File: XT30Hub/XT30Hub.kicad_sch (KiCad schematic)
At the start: 12 parts, among them J1 Conn_01x02, J2 Conn_01x02, J3 Conn_01x02, J4 Conn_01x02, J5 Conn_01x02, J6 Conn_01x02

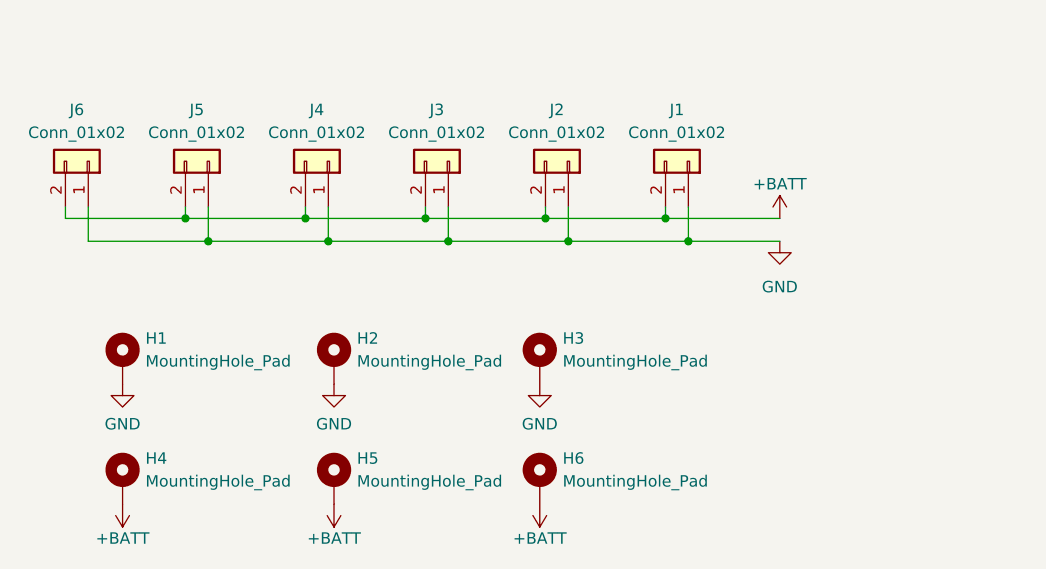
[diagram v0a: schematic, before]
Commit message: [XT30Hub] : 回路図をPDF化
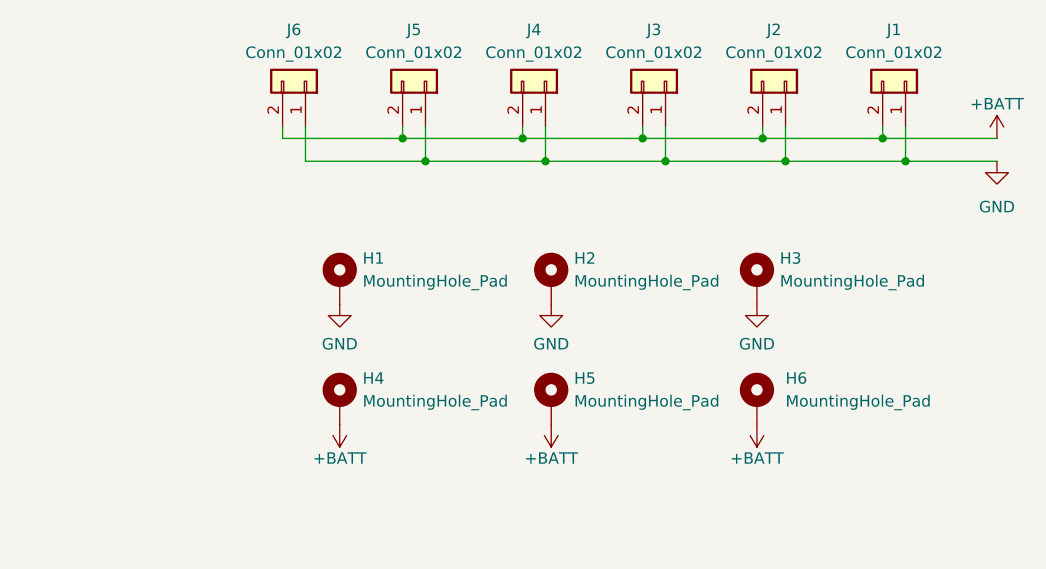
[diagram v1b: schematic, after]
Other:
- moved on the sheet: H1, H2, H3, H4, H5, H6, J1, J2, J3, J4, J5, J6
